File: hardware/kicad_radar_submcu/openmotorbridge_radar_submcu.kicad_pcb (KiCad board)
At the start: 2 copper layers, 115 x 65 mm, 56 parts, among them J1 12V_RADAR_PWR, J2 JST_SH_4P_MR20, J3 PROG_UART_4P, J4 Taoglas_FXUWB10, SW1 BOOT_SW, SW2 RESET_SW, U1 ESP32-C5-WROOM-1U, U2 TPS7A0533, U3 DW3110, Y1_UWB 38.4MHz

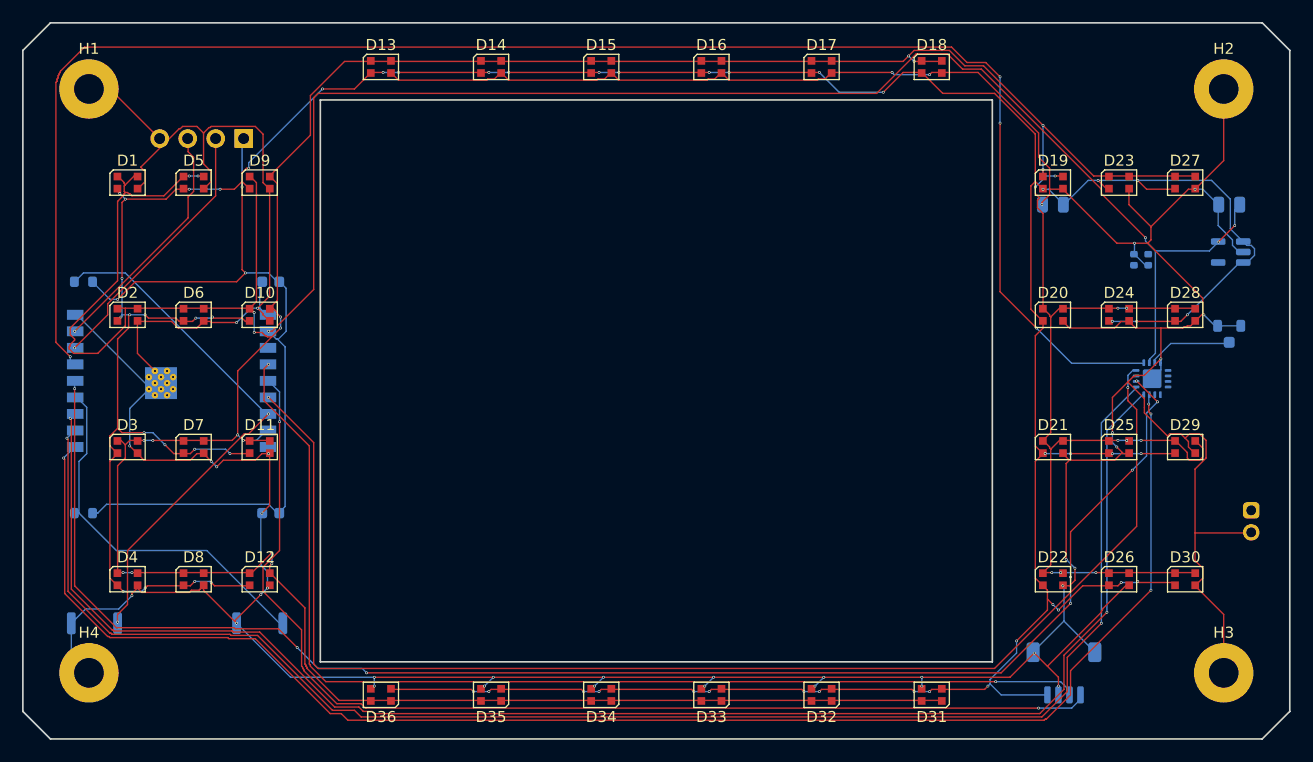
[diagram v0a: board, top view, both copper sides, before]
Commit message: fix(hardware): fleet-wide 7-PCBA remediation, schematic parity & doc alignment
- PCBA 01 (Central Box): Synchronized DTM-12 schematic and PCB routing, purged obsolete analog audio transformers/HD26 connector.
- PCBA 03 (Smart Cartridge): Verified Kelvin ground isolation on J_AUDIO_PWR, resolved U1.16 BAY_SELECT single net.
- PCBA 05 (Front Node): Mapped DW3110 UWB SPI/IRQ/RST to ESP32-S3 pads 30-35, connected MK1 I2S MEMS mic and Y_UWB crystal.
- PCBA 07 (Smart Keyfob): Connected 12 unrouted signals (SX1262 LoRa SPI, DRV2605L I2C, SWD, RTC crystal, buttons) to nRF52840 pads.
- PCBA 08 (Radar Sub-MCU): Synchronized J1.1 power rail to VCC_5V, connected Y1_UWB crystal to DW3110 pads 4 & 5.
- PCBA 09 & PCBA 10 (OMM 2.4 GHz & 446 MHz): Verified 4-layer stackup, BQ24075 ground ties, SA818 isolation, and vertical B.Cu J_HELMET orientation.
- Tools: Added verify_hardware_integrity.py with automated DRC/parity/single-net/floating-pad checks (all 7 PCBAs HEALTHY).
- Docs: Synchronized docs/de and docs/en hardware specifications, pinouts, and DTM-12 architecture.
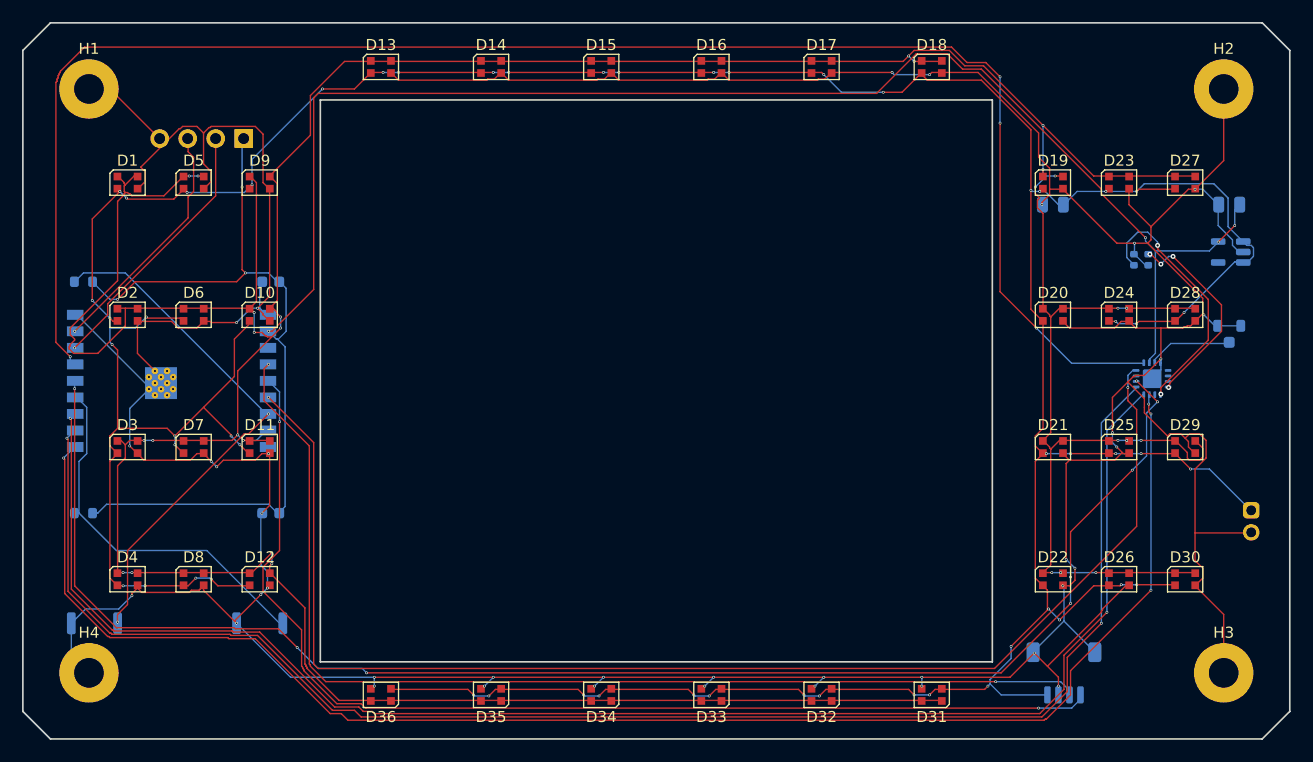
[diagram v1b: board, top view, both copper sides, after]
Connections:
- J1 pad 1: RADAR_PWR_12V -> VCC_5V
- U3 pad 4: (no net) -> UWB_XTAL1
- U3 pad 5: (no net) -> UWB_XTAL2
- Y1_UWB pad 1: (no net) -> UWB_XTAL1
- Y1_UWB pad 3: (no net) -> UWB_XTAL2
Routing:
- net VCC_5V: track 355.7 -> 379.6 mm, vias 56 -> 55
- net UWB_XTAL2: track 0.00 -> 23.4 mm, vias 0 -> 2
- net UWB_XTAL1: track 0.00 -> 18.6 mm, vias 0 -> 4
